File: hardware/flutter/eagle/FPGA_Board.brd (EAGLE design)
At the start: 100 x 77 mm, 61 parts, among them IC1 AT45DB161D-SU, IC2 MEGA8-AI, IC3 MAX481CSA, Q1 8Mhz, U2 XC3S50AVQ100

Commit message: update of flutter: didn't know what i have done....
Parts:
- added R20: 10k, resistor:M0805
- added X1: BU-SMA-V, con-coax:BU-SMA-V
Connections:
- new net GPS_NRESET: IC2.9, R20.2, U$6.NRESET
- new net GPS_RX: IC2.11, U$6.RXDA
- new net GPS_TX: IC2.10, U$6.TXDA
- new net N$14: U$6.EX_ANT, X1.1
- net GND: now also R20.1, U$6.GND1, U$6.GND2, U$6.GND3, U$6.GND4, U$6.RTCM, X1.2, X1.3, X1.4, X1.5
- net PPS: now also U$6.1PPS
- net VCC3.3: now also U$6.VBACKUP, U$6.VCC
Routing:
- net PPS: track 52.7 -> 119.9 mm
- net GPS_NRESET: track 0.00 -> 36.2 mm, vias 0 -> 2
- net N$14: track 0.00 -> 28.9 mm, vias 0 -> 1
- net VCC3.3: track 273.7 -> 301.6 mm
- net GPS_RX: track 0.00 -> 21.5 mm, vias 0 -> 2
- net GPS_TX: track 0.00 -> 21.3 mm, vias 0 -> 2
- net GND: track 691.5 -> 693.7 mm

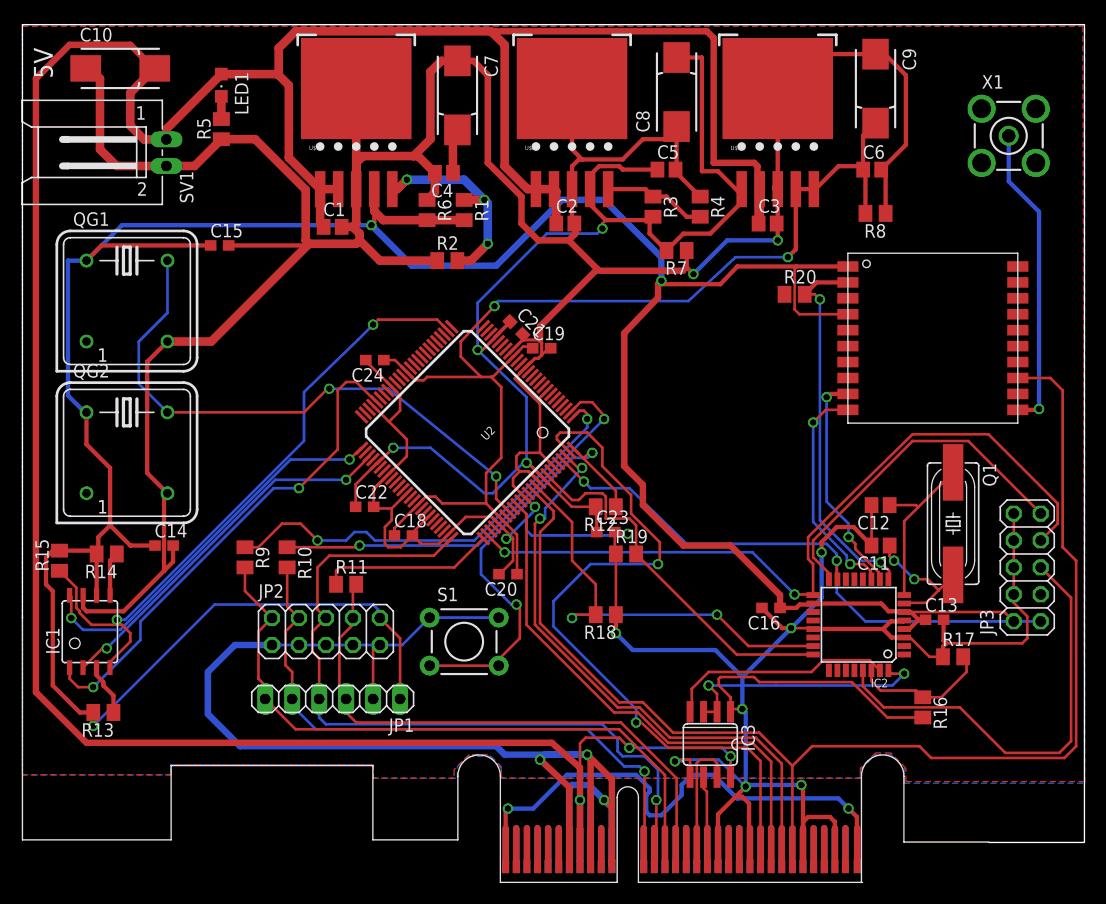
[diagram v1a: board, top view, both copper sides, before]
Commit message: Added testpoints
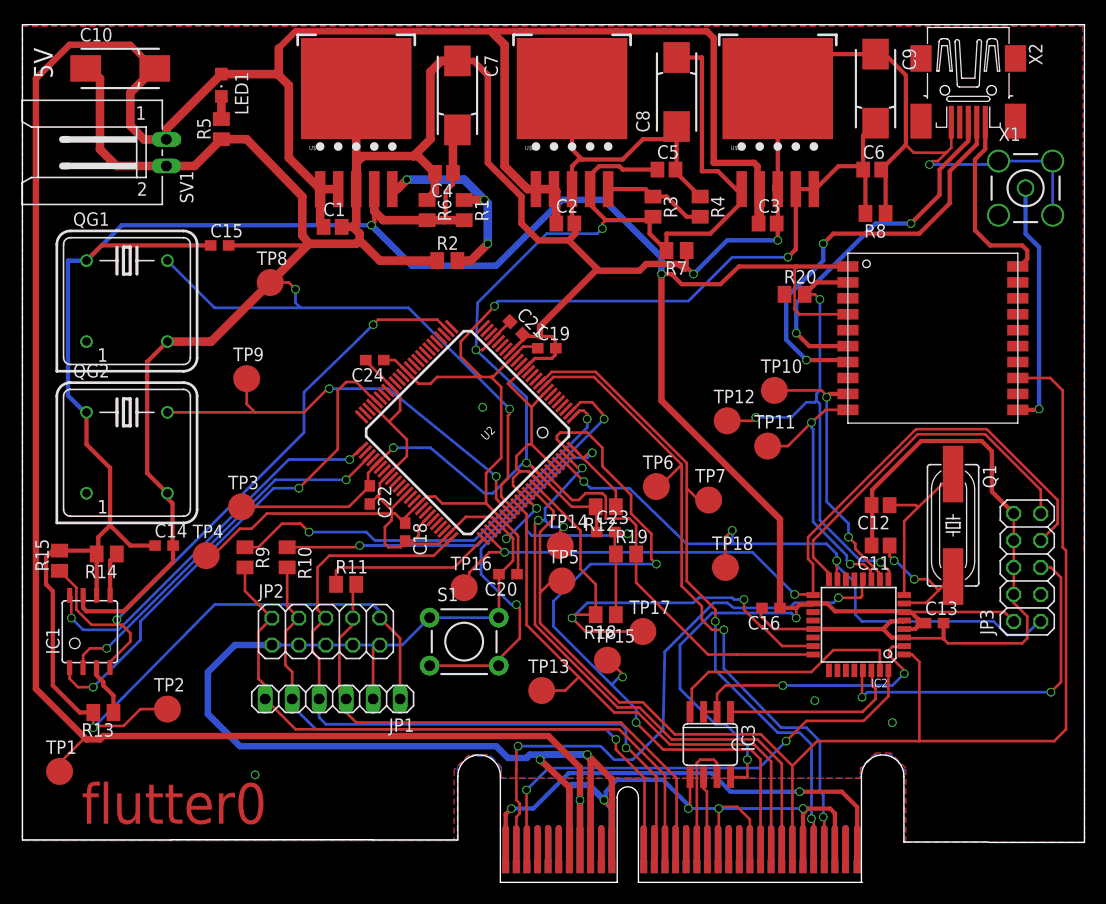
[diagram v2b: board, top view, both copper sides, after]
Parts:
- removed R16: 1k, resistor:M0805
- removed R17: 1.6k, resistor:M0805
- added TP1, TP10, TP11, TP12, TP13, TP14, TP15, TP16, TP17, TP18, TP2, TP3, TP4, TP5, TP6, TP7, TP8, TP9: TPB2,54, testpad:B2,54
- added X2: MINI-USB-32005-201, con-cypressindustries:32005-201
- moved U$5 44.6 mm to (50.2, 51.3)
- moved X1 5.17 mm to (94.5, 64.6)
- moved C22 1.21 mm to (32.7, 35.7), turned to 270 degrees
- moved C19 0.48 mm to (49.4, 49.5)
- moved C18 0.35 mm to (36.0, 32.2), turned to 270 degrees
- moved C13 0.32 mm to (85.9, 23.7)
- moved Q1 0.16 mm to (87.6, 32.9)
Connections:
- net N$6 renamed DI
- removed net N$10: IC3.1, R16.2
- removed net N$9: IC2.30, R16.1, R17.2
- new net CS: IC2.32, U$4.A03(/CS,IRQ)
- new net D+: U$6.DPLUSE, X2.3
- new net D-: U$6.DMINUS, X2.2
- new net DO: IC2.30, IC3.1
- new net IRQ: IC2.12, U$4.A02(IRQ)
- new net N$15: X2.4
- new net TIMING_CLK: QG1.5, TP8.TP, U2.P84
- new net USBVCC: U$6.USB-VCC, X2.1
- net +5V: now also TP1.TP; no longer IC3.8
- net FASTCLK+: now also TP6.TP, U2.P9
- net FASTCLK-: now also TP7.TP, U2.P10
- net FPGA_SPI_CLOCK: now also TP9.TP; no longer QG1.5
- net GND: now also X2.5; no longer R17.1
- net GPS_NRESET: now also TP12.TP
- net GPS_RX: now also TP11.TP
- net GPS_TX: now also TP10.TP
- net N$5: now also IC2.2; no longer IC2.32
- net PPS: now also IC2.1, TP5.TP
- net SLOWCLK/CLK: now also TP13.TP
- net SLOWCLK/CS: now also TP14.TP
- net SLOWCLK/MOSI: now also TP15.TP
- net UC_FPGA_SPI_CS: now also TP17.TP
- net UC_MOSI: now also TP18.TP
- net UC_SCK: now also TP16.TP
- net VCC1.2: now also TP4.TP
- net VCC2.5: now also TP3.TP
- net VCC3.3: now also IC3.8, TP2.TP
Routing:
- net FASTCLK+: track 0.00 -> 65.5 mm, vias 0 -> 2
- net FASTCLK-: track 0.00 -> 64.5 mm, vias 0 -> 2
- net IRQ: track 0.00 -> 57.0 mm, vias 0 -> 2
- net TIMING_CLK: track 0.00 -> 52.8 mm, vias 0 -> 2
- net CS: track 0.00 -> 47.4 mm, vias 0 -> 2
- net D-: track 0.00 -> 39.3 mm, vias 0 -> 2
- net VCC3.3: track 301.6 -> 339.9 mm, vias 3 -> 5
- net D+: track 0.00 -> 33.9 mm, vias 0 -> 2
- net N$10: track 24.4 -> 0.00 mm
- net VCC1.2: track 110.0 -> 130.1 mm
- net USBVCC: track 0.00 -> 18.9 mm
- net DO: track 0.00 -> 17.0 mm
- net +5V: track 294.1 -> 279.0 mm, vias 3 -> 1
- net N$9: track 13.2 -> 0.00 mm
- net FPGA_SPI_CLOCK: track 55.2 -> 42.2 mm
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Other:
- board text added: "flutter0"

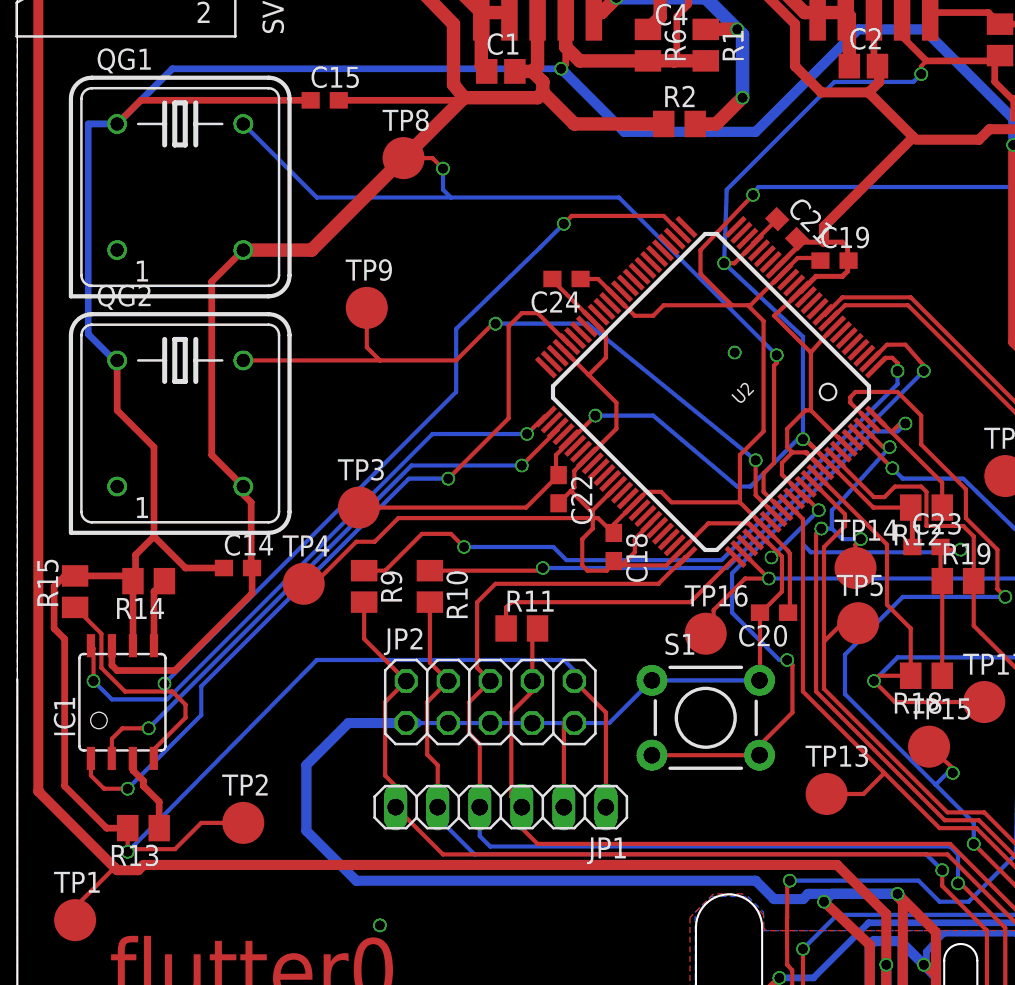
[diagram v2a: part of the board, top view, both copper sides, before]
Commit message: added pinheader to access fpga's eeprom pins
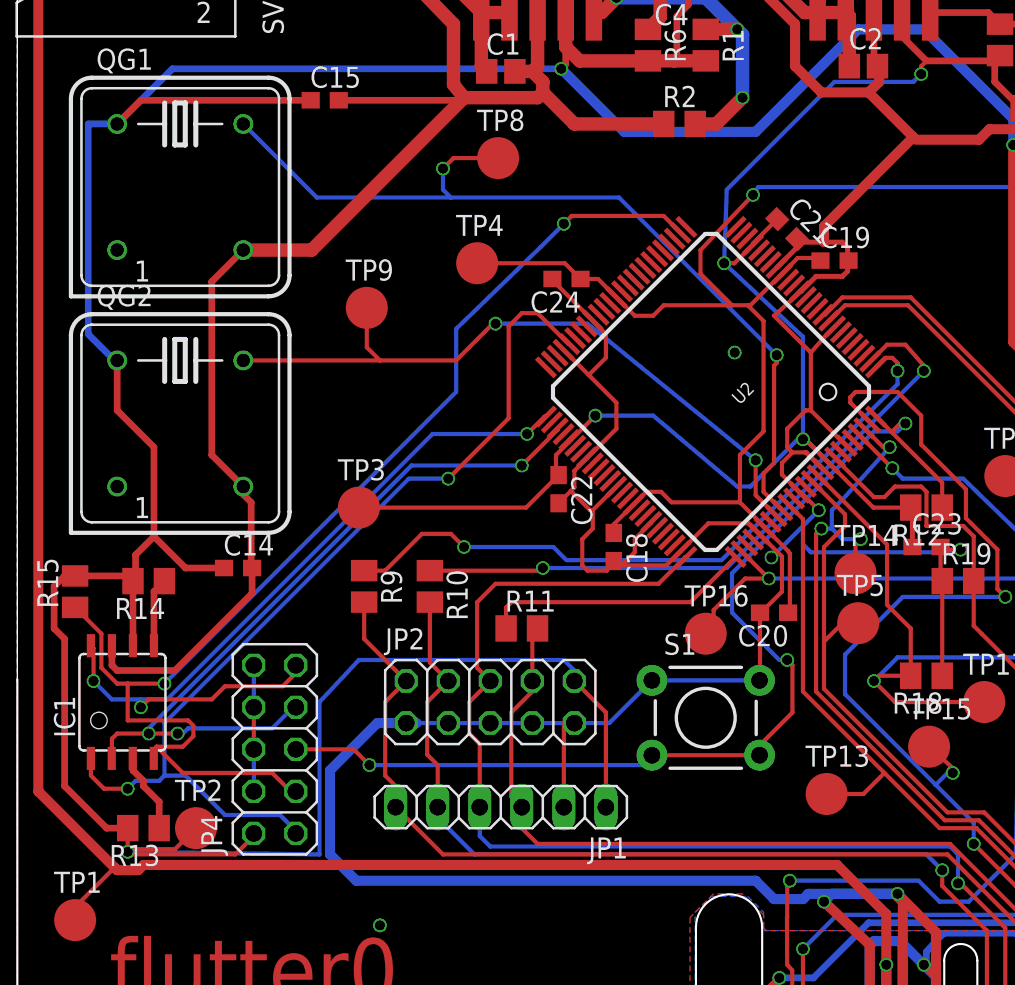
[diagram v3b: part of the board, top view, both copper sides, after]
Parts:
- added JP4: ISP, pinhead:2X05
- moved TP4 22.0 mm to (27.8, 49.4)
- moved TP8 5.71 mm to (29.1, 55.7)
- moved TP2 2.88 mm to (10.8, 15.2)
- moved TP14 0.32 mm to (50.6, 30.6)
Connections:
- net CS_EEPROM: now also JP4.3
- net GND: now also JP4.10, JP4.4, JP4.6, JP4.8
- net MISO_EEPROM: now also JP4.9
- net MOSI_EEPROM: now also JP4.1
- net PROG_B: now also JP4.5
- net SCK_EEPROM: now also JP4.7
- net VCC3.3: now also JP4.2
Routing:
- net PROG_B: track 42.5 -> 64.7 mm, vias 2 -> 3
- net VCC1.2: track 130.1 -> 116.0 mm
- net CS_EEPROM: track 60.3 -> 73.8 mm
- net VCC3.3: track 339.9 -> 351.2 mm
- net MISO_EEPROM: track 37.1 -> 48.2 mm, vias 2 -> 3
- net MOSI_EEPROM: track 47.2 -> 57.5 mm
- net SCK_EEPROM: track 35.9 -> 45.7 mm, vias 2 -> 3
- net GND: track 697.7 -> 703.1 mm
- net TIMING_CLK: track 52.8 -> 53.7 mm

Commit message: testpads are 20% cooler now!
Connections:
- removed net FASTCLK3V3: U$4.A31(FASTCLK3V3)
- net FASTCLK+: now also U$4.A31(FASTCLK3V3)
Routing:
- net FASTCLK+: track 65.5 -> 72.2 mm, vias 2 -> 3
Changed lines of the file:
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@@
 <wire x1="59.69" y1="36.5125" x2="60.0075" y2="36.5125" width="0.254" layer="1"/>
 <wire x1="60.0075" y1="36.5125" x2="62.07125" y2="38.57625" width="0.254" layer="1"/>
+<contactref element="U$4" pad="A31(FASTCLK3V3)"/>
+<wire x1="77.5" y1="0.74" x2="77.47" y2="0.74" width="0.254" layer="1"/>
+<wire x1="77.47" y1="0.74" x2="77.47" y2="5.3975" width="0.254" layer="1"/>
+<via x="77.47" y="5.3975" extent="1-16" drill="0.6" shape="octagon"/>
+<wire x1="77.47" y1="5.3975" x2="75.40625" y2="5.3975" width="0.254" layer="16"/>
 <wire x1="49.05375" y1="45.87875" x2="49.051778125" y2="45.90585" width="0" layer="19" extent="1-1"/>
 </signal>
@@
 <wire x1="62.5475" y1="27.6225" x2="62.5475" y2="36.35375" width="0.254" layer="1"/>
 <wire x1="62.5475" y1="38.735" x2="53.975" y2="47.3075" width="0.254" layer="1"/>
-<wire x1="53.975" y1="47.3075" x2="49.8475" y2="47.3075" width="0.254" layer="1"/>
-<wire x1="49.8475" y1="47.3075" x2="48.799403125" y2="46.259403125" width="0.254" layer="1"/>
-<wire x1="48.799403125" y1="46.259403125" x2="48.698225" y2="46.259403125" width="0.254" layer="1"/>
+<wire x1="53.975" y1="47.3075" x2="49.68875" y2="47.3075" width="0.254" layer="1"/>
+<wire x1="49.68875" y1="47.3075" x2="48.799403125" y2="46.418153125" width="0.254" layer="1"/>
+<wire x1="48.799403125" y1="46.418153125" x2="48.698225" y2="46.259403125" width="0.254" layer="1"/>
 <contactref element="TP7" pad="TP"/>
 <wire x1="64.61125" y1="35.2425" x2="63.65875" y2="35.2425" width="0.254" layer="1"/>
 <wire x1="63.65875" y1="35.2425" x2="62.5475" y2="36.35375" width="0.254" layer="1"/>
 <wire x1="62.5475" y1="36.35375" x2="62.5475" y2="38.735" width="0.254" layer="1"/>
-</signal>
-<signal name="FASTCLK3V3">
-<contactref element="U$4" pad="A31(FASTCLK3V3)"/>
 </signal>
 <signal name="TRST">
@@
 </signal>
 </signals>
-<errors>
-</errors>
 </board>
 </drawing>

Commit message: routes are 20% cooler now
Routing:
- net VCC3.3: track 351.2 -> 354.1 mm
- net GND: track 703.1 -> 705.6 mm, vias 16 -> 17
- net FPGA_SPI_CLOCK: track 42.2 -> 42.8 mm
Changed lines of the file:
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@@
 <wire x1="71.12" y1="59.69" x2="66.3575" y2="59.69" width="0.4064" layer="16"/>
 <wire x1="66.3575" y1="59.69" x2="63.1825" y2="56.515" width="0.4064" layer="16"/>
-<via x="63.1825" y="56.515" extent="1-16" drill="0.6" shape="square"/>
+<via x="63.1825" y="56.515" extent="1-16" drill="0.6" shape="octagon"/>
 <wire x1="63.1825" y1="56.515" x2="63.1775" y2="56.515" width="0.4064" layer="1"/>
 <wire x1="63.1775" y1="56.515" x2="62.545" y2="57.1475" width="0.4064" layer="1"/>
@@
 <wire x1="14.2875" y1="20.0025" x2="14.2875" y2="22.5425" width="0.254" layer="1"/>
 <wire x1="14.2875" y1="22.5425" x2="14.2875" y2="25.0825" width="0.254" layer="16"/>
+<wire x1="71.7575" y1="54.61" x2="70.32625" y2="54.61" width="0.4064" layer="1"/>
+<wire x1="70.32625" y1="54.61" x2="70.32625" y2="55.5625" width="0.4064" layer="1"/>
+<via x="70.32625" y="55.5625" extent="1-16" drill="0.6" shape="octagon"/>
+<wire x1="70.32625" y1="55.5625" x2="70.32625" y2="55.40375" width="0.4064" layer="16"/>
 </signal>
 <signal name="+5V">
@@
 <wire x1="71.335" y1="33.44" x2="60.16625" y2="44.60875" width="0.6096" layer="1"/>
 <wire x1="60.16625" y1="44.60875" x2="60.16625" y2="56.515" width="0.6096" layer="1"/>
-<via x="60.16625" y="56.515" extent="1-16" drill="0.6" shape="square"/>
+<via x="60.16625" y="56.515" extent="1-16" drill="0.6" shape="octagon"/>
 <wire x1="60.16625" y1="56.515" x2="60.16625" y2="58.1025" width="0.6096" layer="16"/>
 <wire x1="60.16625" y1="58.1025" x2="54.76875" y2="63.5" width="0.6096" layer="16"/>
@@
 <contactref element="U$6" pad="VCC"/>
 <contactref element="U$6" pad="VBACKUP"/>
-<wire x1="77.725" y1="57.2325" x2="72.86625" y2="57.2325" width="0.4064" layer="1"/>
-<wire x1="72.86625" y1="57.2325" x2="67.46875" y2="57.2325" width="0.4064" layer="1"/>
+<wire x1="77.725" y1="57.2325" x2="69.215" y2="57.2325" width="0.4064" layer="1"/>
+<wire x1="69.215" y1="57.2325" x2="67.46875" y2="57.2325" width="0.4064" layer="1"/>
 <wire x1="67.46875" y1="57.2325" x2="65.7225" y2="55.5625" width="0.4064" layer="1"/>
 <wire x1="65.7225" y1="55.5625" x2="62.07125" y2="55.5625" width="0.4064" layer="1"/>
 <wire x1="62.07125" y1="55.5625" x2="61.11875" y2="56.515" width="0.4064" layer="1"/>
 <wire x1="61.11875" y1="56.515" x2="60.16625" y2="56.515" width="0.4064" layer="1"/>
-<wire x1="77.725" y1="52.7325" x2="73.15625" y2="52.7325" width="0.254" layer="1"/>
-<wire x1="73.15625" y1="52.7325" x2="72.7075" y2="53.18125" width="0.254" layer="1"/>
-<wire x1="72.7075" y1="53.18125" x2="72.7075" y2="57.07375" width="0.254" layer="1"/>
-<wire x1="72.7075" y1="57.07375" x2="72.86625" y2="57.2325" width="0.254" layer="1"/>
+<wire x1="77.725" y1="52.7325" x2="70.4575" y2="52.7325" width="0.254" layer="1"/>
+<wire x1="70.4575" y1="52.7325" x2="69.215" y2="53.975" width="0.254" layer="1"/>
+<wire x1="69.215" y1="53.975" x2="69.215" y2="57.2325" width="0.254" layer="1"/>
 <contactref element="IC3" pad="8"/>
 <wire x1="66.675" y1="9.15035" x2="68.2625" y2="9.15035" width="0.254" layer="1"/>
@@
 <via x="34.925" y="40.16375" extent="1-16" drill="0.6" shape="octagon"/>
 <wire x1="34.925" y1="40.16375" x2="38.4175" y2="40.16375" width="0.254" layer="16"/>
-<wire x1="38.4175" y1="40.16375" x2="43.4975" y2="35.8775" width="0.254" layer="16"/>
-<wire x1="43.4975" y1="35.8775" x2="44.29125" y2="35.8775" width="0.254" layer="16"/>
+<wire x1="38.4175" y1="40.16375" x2="42.70375" y2="35.8775" width="0.254" layer="16"/>
+<wire x1="42.70375" y1="35.8775" x2="44.29125" y2="35.8775" width="0.254" layer="16"/>
 <wire x1="44.29125" y1="35.8775" x2="47.14875" y2="38.735" width="0.254" layer="16"/>
 <wire x1="47.14875" y1="38.735" x2="47.46625" y2="38.735" width="0.254" layer="16"/>
@@
 <wire x1="41.275" y1="48.73625" x2="41.275" y2="50.165" width="0.254" layer="1"/>
 <wire x1="41.275" y1="50.165" x2="44.45" y2="53.49875" width="0.254" layer="1"/>
-<via x="72.0725" y="58.1025" extent="1-16" drill="0.6" shape="square"/>
+<via x="72.0725" y="58.1025" extent="1-16" drill="0.6" shape="octagon"/>
 <wire x1="72.0725" y1="58.1025" x2="66.83375" y2="58.1025" width="0.254" layer="16"/>
 <wire x1="66.83375" y1="58.1025" x2="62.70625" y2="53.975" width="0.254" layer="16"/>
@@
 <contactref element="QG2" pad="5"/>
 <contactref element="U2" pad="P83"/>
-<wire x1="34.44875" y1="45.72" x2="44.60875" y2="37.465" width="0.254" layer="16"/>
+<wire x1="36.195" y1="45.87875" x2="44.60875" y2="37.465" width="0.254" layer="16"/>
 <via x="44.60875" y="37.465" extent="1-16" drill="0.6" shape="octagon"/>
 <wire x1="44.60875" y1="37.465" x2="44.60875" y2="35.3582125" width="0.254" layer="1"/>
@@
 <wire x1="28.73375" y1="45.72" x2="28.8925" y2="45.72" width="0.254" layer="1"/>
 <via x="28.8925" y="45.72" extent="1-16" drill="0.6" shape="octagon"/>
-<wire x1="28.8925" y1="45.72" x2="34.44875" y2="45.72" width="0.254" layer="16"/>
+<wire x1="28.8925" y1="45.72" x2="36.195" y2="45.87875" width="0.254" layer="16"/>
 <contactref element="TP9" pad="TP"/>
 <wire x1="21.11375" y1="46.6725" x2="21.11375" y2="44.29125" width="0.254" layer="1"/>
@@
 <wire x1="33.02" y1="51.7525" x2="31.59125" y2="50.32375" width="0.254" layer="16"/>
 <wire x1="31.59125" y1="50.32375" x2="26.51125" y2="45.4025" width="0.254" layer="16"/>
-<wire x1="26.51125" y1="45.4025" x2="26.51125" y2="41.5925" width="0.254" layer="16"/>
-<wire x1="26.51125" y1="41.5925" x2="8.89" y2="23.97125" width="0.254" layer="16"/>
+<wire x1="26.51125" y1="45.4025" x2="26.51125" y2="41.11625" width="0.254" layer="16"/>
+<wire x1="26.51125" y1="41.11625" x2="9.36625" y2="23.97125" width="0.254" layer="16"/>
+<wire x1="9.36625" y1="23.97125" x2="8.89" y2="23.97125" width="0.254" layer="16"/>
 <via x="8.89" y="23.97125" extent="1-16" drill="0.6" shape="octagon"/>
 <wire x1="8.89" y1="23.97125" x2="6.6675" y2="23.97125" width="0.254" layer="1"/>
@@
 <wire x1="73.6575" y1="54.61" x2="74.6125" y2="54.61" width="0.254" layer="1"/>
 <wire x1="74.6125" y1="54.61" x2="75.08875" y2="54.13375" width="0.254" layer="1"/>
-<via x="75.08875" y="54.13375" extent="1-16" drill="0.6" shape="square"/>
+<via x="75.08875" y="54.13375" extent="1-16" drill="0.6" shape="octagon"/>
 <wire x1="75.08875" y1="54.13375" x2="75.08875" y2="45.56125" width="0.254" layer="16"/>
 <wire x1="75.08875" y1="45.56125" x2="74.77125" y2="45.24375" width="0.254" layer="16"/>
@@
 <wire x1="84.455" y1="60.325" x2="76.35875" y2="60.325" width="0.4064" layer="1"/>
 <wire x1="76.35875" y1="60.325" x2="75.40625" y2="59.3725" width="0.4064" layer="1"/>
-<via x="75.40625" y="59.3725" extent="1-16" drill="0.6" shape="square"/>
+<via x="75.40625" y="59.3725" extent="1-16" drill="0.6" shape="octagon"/>
 <wire x1="75.40625" y1="59.3725" x2="75.40625" y2="57.785" width="0.4064" layer="16"/>
 <wire x1="75.40625" y1="57.785" x2="71.91375" y2="54.2925" width="0.4064" layer="16"/>
